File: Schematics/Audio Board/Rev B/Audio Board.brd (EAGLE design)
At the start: 65 x 60 mm, 30 parts, among them IC1 7803, IC2 7810-LDO, IC3 STM32F303CBT7, IC4 AK4430ET, IC5 PCA9600SO8, J1 503398-1892, J2 LINEOUT_R, J3 LINEOUT_L, J4 54602-908LF, J5 54602-908LF, J6 54602-908LF, X2 22-23-2031

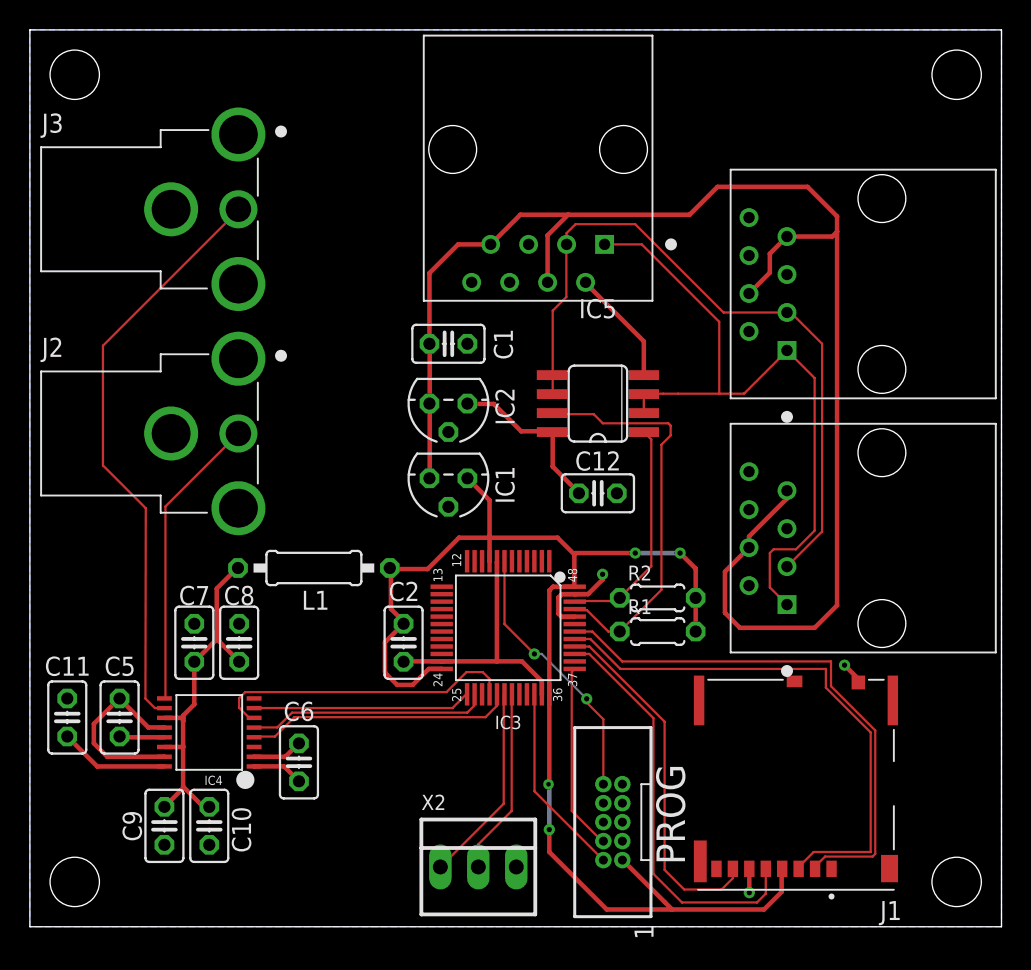
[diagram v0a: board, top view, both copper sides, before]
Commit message: Small changes to Audio Board Rev B and add Gerbers
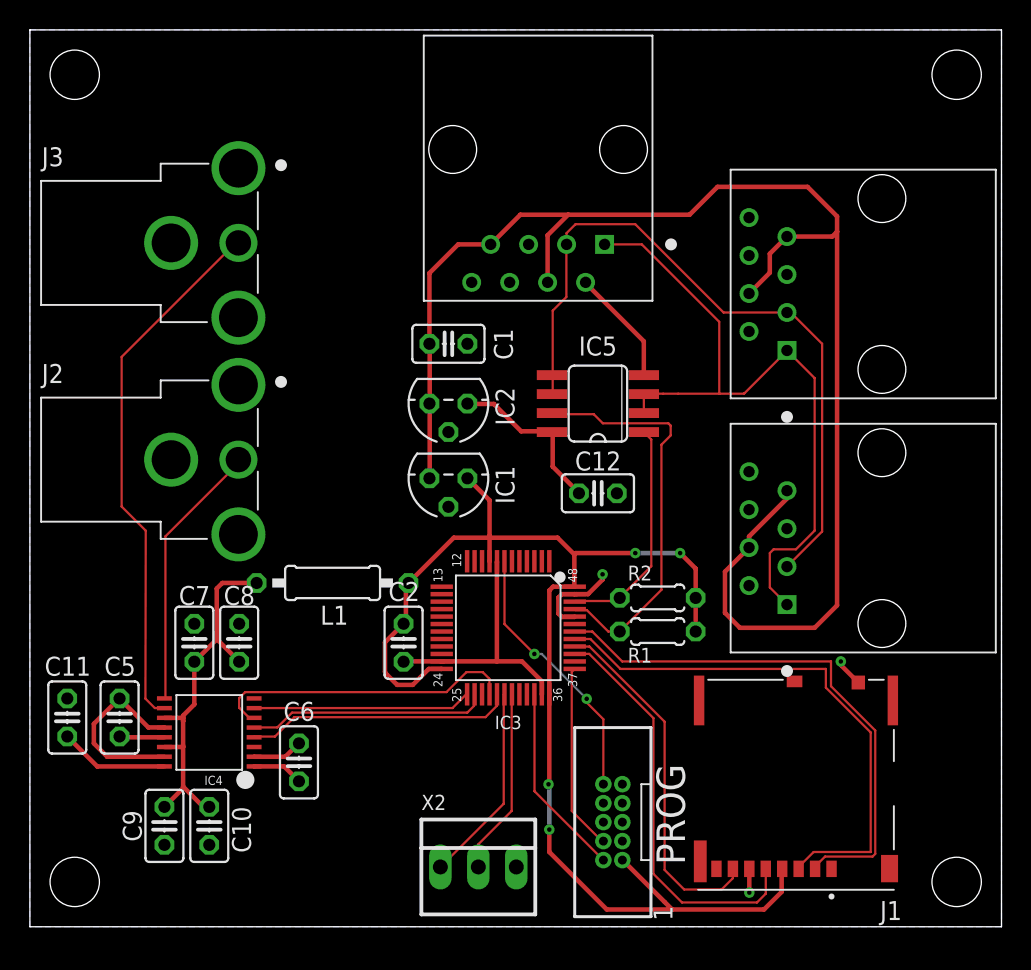
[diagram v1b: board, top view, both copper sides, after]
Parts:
- moved J3 2.25 mm to (8.00, 45.8)
- moved J2 1.75 mm to (8.00, 31.2)
- moved L1 1.60 mm to (20.2, 23.0)
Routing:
- net N$3: track 39.2 -> 36.0 mm
- net VCC: track 90.6 -> 88.5 mm
- net N$4: track 19.8 -> 18.0 mm
- net V+: track 25.7 -> 26.6 mm

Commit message: Minor revisions to Audio Board Rev B
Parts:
- moved C6 0.75 mm to (18.0, 10.2)
- renumbered X2 to SERIAL
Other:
- board text added: "RULOS Audio Synthesizer Rev B April 2019"
- board text added: "TX RX GND"
- board text removed: "RULOS Audio Synthesizer Rev A April 2019"
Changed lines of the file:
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@@
 </polygon>
 <text x="6.75" y="56" size="1.016" layer="51" font="vector">RULOS Audio Synthesizer
-Rev A       April 2019</text>
+Rev B          April 2019</text>
+<text x="26.5" y="7.75" size="0.9" layer="51">TX  RX  GND</text>
 </plain>
 <attributes>
@@
 <attribute name="PRICE" value="None" x="51.25" y="9.5" size="1.778" layer="27" rot="R180" display="off"/>
 </element>
-<element name="X2" library="con-molex" library_urn="urn:adsk.eagle:library:165" package="22-23-2031" package3d_urn="urn:adsk.eagle:package:8078634/1" value="22-23-2031" x="30" y="4" smashed="yes">
+<element name="SERIAL" library="con-molex" library_urn="urn:adsk.eagle:library:165" package="22-23-2031" package3d_urn="urn:adsk.eagle:package:8078634/1" value="22-23-2031" x="30" y="4" smashed="yes">
 <attribute name="MF" value="MOLEX" x="19.84" y="15.43" size="1.778" layer="27" display="off"/>
 <attribute name="MPN" value="22-23-2031" x="19.84" y="15.43" size="1.778" layer="27" display="off"/>
-<attribute name="NAME" x="26.19" y="7.81" size="1.016" layer="25" ratio="10"/>
+<attribute name="NAME" x="26.44" y="9.31" size="1.016" layer="25" ratio="10"/>
 <attribute name="OC_FARNELL" value="1462950" x="19.84" y="15.43" size="1.778" layer="27" display="off"/>
 <attribute name="OC_NEWARK" value="30C0862" x="19.84" y="15.43" size="1.778" layer="27" display="off"/>
@@
 <attribute name="VALUE" x="22.0106" y="25.635" size="1.27" layer="27" ratio="10" rot="R180"/>
 </element>
-<element name="C6" library="rcl" library_urn="urn:adsk.eagle:library:334" package="C025-025X050" package3d_urn="urn:adsk.eagle:package:23629/2" value="1uF" x="18" y="11" smashed="yes" rot="R270">
-<attribute name="NAME" x="16.964" y="13.774" size="1.27" layer="25" ratio="10"/>
-<attribute name="SPICEPREFIX" value="C" x="18" y="11" size="1.778" layer="27" rot="R270" display="off"/>
-<attribute name="VALUE" x="16.754" y="7.016" size="1.27" layer="27" ratio="10"/>
+<element name="C6" library="rcl" library_urn="urn:adsk.eagle:library:334" package="C025-025X050" package3d_urn="urn:adsk.eagle:package:23629/2" value="1uF" x="18" y="10.25" smashed="yes" rot="R270">
+<attribute name="NAME" x="16.964" y="13.024" size="1.27" layer="25" ratio="10"/>
+<attribute name="SPICEPREFIX" value="C" x="18" y="10.25" size="1.778" layer="27" rot="R270" display="off"/>
+<attribute name="VALUE" x="16.754" y="6.266" size="1.27" layer="27" ratio="10"/>
 </element>
 <element name="C11" library="rcl" library_urn="urn:adsk.eagle:library:334" package="C025-025X050" package3d_urn="urn:adsk.eagle:package:23629/2" value="1uF" x="2.5" y="14" smashed="yes" rot="R90">
@@
 <wire x1="27.55" y1="17.25" x2="27.54969375" y2="17.25030625" width="0.3048" layer="1"/>
 <wire x1="27.54969375" y1="17.25030625" x2="26.684265625" y2="17.25030625" width="0.3048" layer="1"/>
-<wire x1="25.615759375" y1="16.1818" x2="26.684265625" y2="17.25030625" width="0.3048" layer="1"/>
+<wire x1="25.865759375" y1="16.4318" x2="26.684265625" y2="17.25030625" width="0.3048" layer="1"/>
 <wire x1="23.753" y1="17.0474" x2="23.821403125" y2="16.928596875" width="0.3048" layer="1"/>
-<wire x1="23.821403125" y1="16.928596875" x2="24.5682" y2="16.1818" width="0.3048" layer="1"/>
-<wire x1="24.5682" y1="16.1818" x2="25.615759375" y2="16.1818" width="0.3048" layer="1"/>
+<wire x1="23.821403125" y1="16.928596875" x2="24.3182" y2="16.4318" width="0.3048" layer="1"/>
+<wire x1="24.3182" y1="16.4318" x2="25.865759375" y2="16.4318" width="0.3048" layer="1"/>
 <wire x1="23.753" y1="19.0286" x2="23.753" y2="17.0474" width="0.3048" layer="1"/>
 <wire x1="24.9936" y1="20.2692" x2="23.753" y2="19.0286" width="0.3048" layer="1"/>
@@
 <contactref element="C2" pad="2"/>
 <contactref element="IC2" pad="2"/>
-<contactref element="X2" pad="3"/>
+<contactref element="SERIAL" pad="3"/>
 <contactref element="IC4" pad="P$15"/>
 <contactref element="C11" pad="2"/>
@@
 <wire x1="8.9916" y1="13.335" x2="9" y2="13.325" width="0.3048" layer="1"/>
 <wire x1="6.096" y1="15.1638" x2="6" y2="15.27" width="0.3048" layer="1"/>
-<wire x1="48.0822" y1="3.81" x2="48.13" y2="3.875" width="0.3048" layer="1"/>
 <wire x1="25.0698" y1="17.7546" x2="27.5082" y2="17.7546" width="0.3048" layer="1"/>
 <wire x1="27.5082" y1="17.7546" x2="27.55" y2="17.75" width="0.3048" layer="1"/>
@@
 </signal>
 <signal name="RX">
-<contactref element="X2" pad="2"/>
+<contactref element="SERIAL" pad="2"/>
 <contactref element="IC3" pad="31"/>
 <wire x1="32.2326" y1="7.7484" x2="32.2326" y2="15.5448" width="0.1524" layer="1"/>
@@
 </signal>
 <signal name="TX">
-<contactref element="X2" pad="1"/>
+<contactref element="SERIAL" pad="1"/>
 <contactref element="IC3" pad="30"/>
 <wire x1="31.6992" y1="8.2296" x2="31.6992" y2="15.5448" width="0.1524" layer="1"/>
@@
 <contactref element="IC3" pad="26"/>
 <contactref element="IC4" pad="P$5"/>
-<wire x1="16.5474" y1="13.335" x2="15.0114" y2="13.335" width="0.1524" layer="1"/>
-<wire x1="17.538" y1="14.3256" x2="16.5474" y2="13.335" width="0.1524" layer="1"/>
-<wire x1="29.2608" y1="14.3256" x2="17.538" y2="14.3256" width="0.1524" layer="1"/>
-<wire x1="29.718" y1="14.7828" x2="29.2608" y2="14.3256" width="0.1524" layer="1"/>
-<wire x1="29.718" y1="15.5448" x2="29.718" y2="14.7828" width="0.1524" layer="1"/>
+<wire x1="15.7974" y1="13.335" x2="15.0114" y2="13.335" width="0.1524" layer="1"/>
+<wire x1="16.073684375" y1="13.611284375" x2="15.7974" y2="13.335" width="0.1524" layer="1"/>
+<wire x1="29.046484375" y1="13.611284375" x2="16.073684375" y2="13.611284375" width="0.1524" layer="1"/>
+<wire x1="29.718" y1="14.2828" x2="29.046484375" y2="13.611284375" width="0.1524" layer="1"/>
+<wire x1="29.718" y1="15.5448" x2="29.718" y2="14.2828" width="0.1524" layer="1"/>
 <wire x1="15.0114" y1="13.335" x2="15" y2="13.325" width="0.1524" layer="1"/>
 <wire x1="29.718" y1="15.5448" x2="29.75" y2="15.55" width="0.1524" layer="1"/>
@@
 <contactref element="IC3" pad="28"/>
 <contactref element="IC4" pad="P$6"/>
-<wire x1="14.6304" y1="14.0208" x2="14.9352" y2="14.0208" width="0.1524" layer="1"/>
-<wire x1="13.9994" y1="14.6518" x2="14.6304" y2="14.0208" width="0.1524" layer="1"/>
-<wire x1="13.9994" y1="15.2948" x2="13.9994" y2="14.6518" width="0.1524" layer="1"/>
+<wire x1="14.3804" y1="14.0208" x2="14.9352" y2="14.0208" width="0.1524" layer="1"/>
+<wire x1="13.9994" y1="14.4018" x2="14.3804" y2="14.0208" width="0.1524" layer="1"/>
+<wire x1="13.9994" y1="15.2948" x2="13.9994" y2="14.4018" width="0.1524" layer="1"/>
 <wire x1="14.4018" y1="15.6972" x2="13.9994" y2="15.2948" width="0.1524" layer="1"/>
 <wire x1="27.8678" y1="15.6972" x2="14.4018" y2="15.6972" width="0.1524" layer="1"/>
@@
 <contactref element="IC3" pad="29"/>
 <contactref element="IC4" pad="P$4"/>
-<wire x1="16.395" y1="12.7254" x2="15.0114" y2="12.7254" width="0.1524" layer="1"/>
-<wire x1="17.6904" y1="14.0208" x2="16.395" y2="12.7254" width="0.1524" layer="1"/>
-<wire x1="30.48" y1="14.0208" x2="17.6904" y2="14.0208" width="0.1524" layer="1"/>
-<wire x1="31.242" y1="14.7828" x2="30.48" y2="14.0208" width="0.1524" layer="1"/>
-<wire x1="31.242" y1="15.5448" x2="31.242" y2="14.7828" width="0.1524" layer="1"/>
-<wire x1="15.0114" y1="12.7254" x2="15" y2="12.675" width="0.1524" layer="1"/>
+<wire x1="29.854309375" y1="12.645109375" x2="15.029890625" y2="12.645109375" width="0.1524" layer="1"/>
+<wire x1="31.242" y1="14.0328" x2="29.854309375" y2="12.645109375" width="0.1524" layer="1"/>
+<wire x1="31.242" y1="15.5448" x2="31.242" y2="14.0328" width="0.1524" layer="1"/>
+<wire x1="15.029890625" y1="12.645109375" x2="15" y2="12.675" width="0.1524" layer="1"/>
 <wire x1="31.242" y1="15.5448" x2="31.25" y2="15.55" width="0.1524" layer="1"/>
 </signal>
@@
 <contactref element="C6" pad="2"/>
 <contactref element="IC4" pad="P$1"/>
-<wire x1="17.010784375" y1="10.726015625" x2="15.001015625" y2="10.726015625" width="0.3048" layer="1"/>
+<wire x1="16.757075" y1="10.726015625" x2="15.001015625" y2="10.726015625" width="0.3048" layer="1"/>
 <wire x1="15" y1="10.725" x2="15.001015625" y2="10.726015625" width="0.3048" layer="1"/>
-<wire x1="17.9832" y1="9.7536" x2="17.010784375" y2="10.726015625" width="0.3048" layer="1"/>
-<wire x1="17.9832" y1="9.7536" x2="18" y2="9.73" width="0.3048" layer="1"/>
+<wire x1="16.757075" y1="10.726015625" x2="18" y2="8.98" width="0.3048" layer="1"/>
 </signal>
 <signal name="V+1">
 <contactref element="C6" pad="1"/>
 <contactref element="IC4" pad="P$2"/>
-<wire x1="17.08874375" y1="11.37374375" x2="15.00125625" y2="11.37374375" width="0.3048" layer="1"/>
+<wire x1="17.58874375" y1="11.37374375" x2="15.00125625" y2="11.37374375" width="0.3048" layer="1"/>
 <wire x1="15" y1="11.375" x2="15.00125625" y2="11.37374375" width="0.3048" layer="1"/>
-<wire x1="17.9832" y1="12.2682" x2="17.08874375" y2="11.37374375" width="0.3048" layer="1"/>
-<wire x1="17.9832" y1="12.2682" x2="18" y2="12.27" width="0.1524" layer="1"/>
+<wire x1="17.8387875" y1="11.6237875" x2="17.58874375" y2="11.37374375" width="0.3048" layer="1"/>
+<wire x1="17.8387875" y1="11.6237875" x2="18" y2="11.52" width="0.1524" layer="1"/>
 </signal>
 <signal name="N$2">
